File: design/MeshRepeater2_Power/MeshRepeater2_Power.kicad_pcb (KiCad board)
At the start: 2 copper layers, 90 x 60 mm, 121 parts, among them J101 INTERBOARD 2x6 VERTICAL, J12 LTO 2S + MID -, J7 SOLAR 12V, J8 Na-ion 1S, Q1 AO3401A, Q4 AO3401A, Q5 BSS138, Q6 AO3401A, Q7 AO3401A, U1 CN3722, U10 LM393XK, U11 LM285Z-2.5G, U12 INA219AIDR, U2 TPS63802DLAR, U8 LMV431A, U9 LMV431A

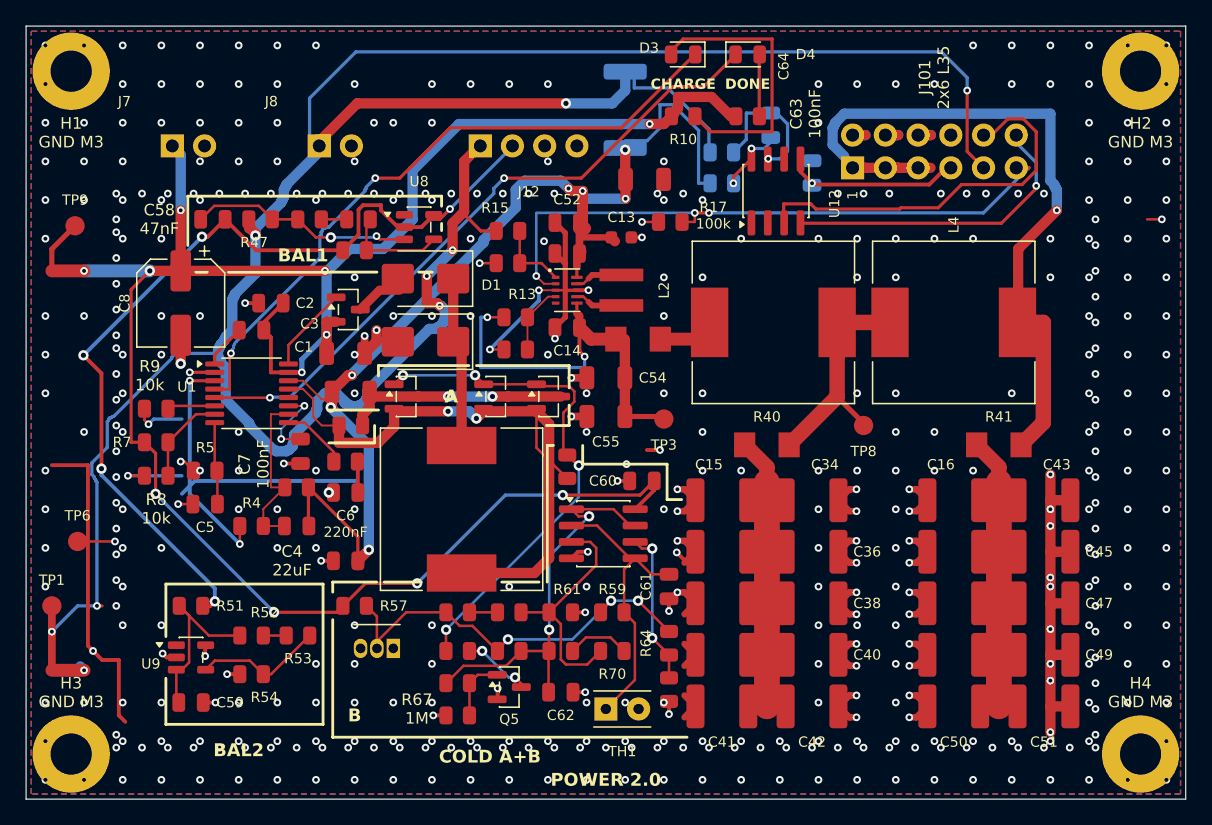
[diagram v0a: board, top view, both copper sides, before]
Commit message: Publish Mesh Repeater 2.0 A3 prototype and engineering audit
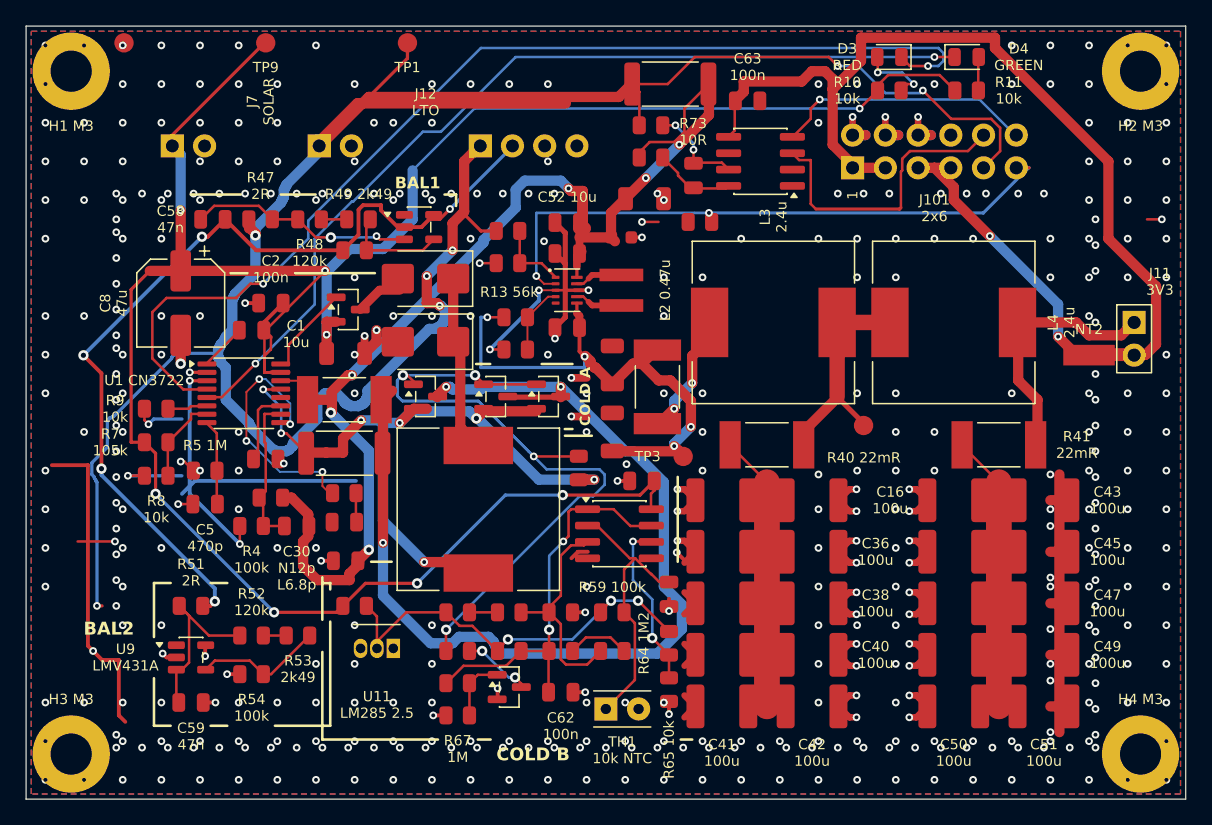
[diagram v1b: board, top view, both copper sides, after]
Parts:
- added J11: LC OUT - 3V3, Meshcore:Connfly_DS1022_1x02RUF11_B_Horizontal, F.Cu at (86.0, 23.0)
- added NT2: 3V3 STAR, Meshcore:NetTie_2_SMD_Power_Star_A3, F.Cu at (82.5, 25.5)
- C63, C64, R72, R73: moved to F.Cu
- J12: value LTO 2S + MID - -> LTO
- J8: value Na-ion 1S -> Na-ion
- R1: footprint Meshcore:R_1206_3216Metric__V2_R1 -> Meshcore:R_Vishay_WSL2512_A3__A3_R1
- R40: footprint Meshcore:R_Vishay_WSL1206_18__V2_R40 -> Meshcore:R_Vishay_WSL2512_A3__A3_R40
- R41: footprint Meshcore:R_Vishay_WSL1206_18__V2_R41 -> Meshcore:R_Vishay_WSL2512_A3__A3_R41
- R55: footprint Meshcore:R_Vishay_WSL1206_18__V2_R55 -> Meshcore:R_Vishay_WSL2512_A3__A3_R55
- R56: value 1.8 ohm 1% 0.125W -> 1.8R 1% 1W; footprint Meshcore:R_0805_2012Metric__V2_R56 -> Meshcore:R_2512_6332Metric__A3_R56
- R71: footprint Meshcore:R_2512_6332Metric__V2_R71 -> Meshcore:R_2512_6332Metric__A3_R71; moved to F.Cu
- TP1: footprint Meshcore:TestPoint_Pad_D1.5mm__V2_TP1 -> Meshcore:TestPoint_Pad_D1p5mm_A3_Edge_R0p9
- TP6: footprint Meshcore:TestPoint_Pad_D1.5mm__V2_TP6 -> Meshcore:TestPoint_Pad_D1p5mm_A3_Edge_R0p9
- TP9: footprint Meshcore:TestPoint_Pad_D1.5mm__V2_TP9 -> Meshcore:TestPoint_Pad_D1p5mm_A3_Edge_R0p9
- moved TP1 51.7 mm to (29.6, 1.30)
- moved TP6 38.9 mm to (7.60, 1.30)
- moved TP9 20.5 mm to (18.6, 1.30)
- moved R11 17.1 mm to (73.0, 5.00)
- moved D4 17.0 mm to (73.0, 2.40)
- moved R10 16.1 mm to (67.0, 5.00)
- moved D3 16.0 mm to (67.0, 2.40)
- moved C63 7.51 mm to (56.0, 5.80), turned to 0 degrees
- moved C64 7.16 mm to (51.8, 11.6)
- moved R73 5.89 mm to (48.5, 7.70)
- moved R72 5.85 mm to (48.5, 10.2)
- moved R71 4.03 mm to (50.0, 4.50), turned to 180 degrees
- moved R55 3.99 mm to (49.0, 28.0), turned to -90 degrees
- moved TP3 3.26 mm to (51.0, 33.4)
- moved C7 2.77 mm to (18.6, 33.6), turned to 0 degrees
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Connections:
- J101 pad 1: FILTER_OUT -> SYS_3V3
- J101 pad 3: FILTER_OUT -> SYS_3V3
- J101 pad 5: FILTER_OUT -> RADIO_3V3
- J101 pad 7: SYS_3V3 -> RADIO_3V3
- J101 pad 8: GND -> unconnected-(J101-NC-Pad8)
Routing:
- net CHG_CS_M: track 17.8 -> 80.7 mm, vias 2 -> 3
- net SYS_3V3: track 13.8 -> 73.5 mm, vias 1 -> 0
- net FILTER_OUT: track 58.9 -> 19.9 mm, vias 1 -> 0
- net CHRG: track 51.3 -> 84.0 mm
- net CHG_G_SHUNT: track 40.2 -> 69.9 mm
- net BAT: track 213.4 -> 191.0 mm, vias 9 -> 7
- net SOLAR: track 165.7 -> 188.1 mm, vias 11 -> 8
- net RADIO_3V3: track 0.00 -> 21.6 mm, vias 0 -> 2
- net DONE: track 51.8 -> 72.0 mm
- net Net-(D3-A): track 22.2 -> 5.58 mm, vias 0 -> 2
- net Net-(U1-COM2): track 5.21 -> 19.8 mm, vias 0 -> 4
- net /2. Converter/SYS_PRE: track 31.3 -> 41.6 mm, vias 2 -> 4
- net CS_P: track 50.8 -> 60.3 mm, vias 2 -> 7
- net SDA: track 30.6 -> 23.1 mm
- net BAT_SYS: track 91.7 -> 99.0 mm, vias 7 -> 6
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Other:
- board text added: "1 BAT 2 MID 3 GND 4 NC"
- board text added: "C1 10u"
- board text added: "C12 10u"
- board text added: "C13 100n"
- board text added: "C14 22u"
- board text added: "C15 100u"
- board text added: "C16 100u"
- board text added: "C2 100n"
- board text added: "C3 100n"
- board text added: "C30 N12p L6.8p"
- board text added: "C34 100u"
- board text added: "C35 100u"
- board text added: "C36 100u"
- board text added: "C37 100u"
- board text added: "C38 100u"
- board text added: "C39 100u"
- board text added: "C4 22u"
- board text added: "C40 100u"
- board text added: "C41 100u"
- board text added: "C42 100u"
- board text added: "C43 100u"
- board text added: "C44 100u"
- board text added: "C45 100u"
- board text added: "C46 100u"
- board text added: "C47 100u"
- board text added: "C48 100u"
- board text added: "C49 100u"
- board text added: "C5 470p"
- board text added: "C50 100u"
- board text added: "C51 100u"
- board text added: "C52 10u"
- board text added: "C53 DNP"
- board text added: "C54 DNP"
- board text added: "C55 DNP"
- board text added: "C58 47n"
- board text added: "C59 47n"
- board text added: "C6 220n"
- board text added: "C60 100n"
- board text added: "C61 1n"
- board text added: "C62 100n"
- board text added: "C63 100n"
- board text added: "C64 100n"
- board text added: "C7 100n"
- board text added: "C8 47u"
- board text added: "COLD A"
- board text added: "COLD B"
- board text added: "H1 M3"
- board text added: "H2 M3"
- board text added: "H3 M3"
- board text added: "H4 M3"
- board text added: "J101 1/3 SYS 5/7 RADIO 2/4/6 GND 8 NC 9 BAT 10 SDA 11 MODE 12 SCL"
- board text added: "J101 2x6"
- board text added: "J11 1 LC 2 3V3"
- board text added: "J11 3V3"
- board text added: "J12 LTO"
- board text added: "J7 SOLAR 1 VIN 2 GND"
- board text added: "J8 Na-ion"
- board text added: "J8 Na-ion 1 BAT+ 2 GND"
- board text added: "L1 100u"
- board text added: "L2 0.47u"
- board text added: "L3 2.4u"
- board text added: "L4 2.4u"
- board text added: "Mesh Repeater ver 2.0 Designed by @Alksndritm"
- board text added: "N: Na-ion / L: LTO 2S"
- board text added: "NT2"
- board text added: "Q4 AO34 01A"
- board text added: "Q6 AO34 01A"
- board text added: "Q7 AO34 01A"
- board text added: "R1 0R28"
- board text added: "R15 N40k2 L130k"
- board text added: "R16 49k9"
- board text added: "R3 N61k9 L121k"
- board text added: "R4 100k"
- board text added: "R49 2k49"
- board text added: "R53 2k49"
- board text added: "R56 1R8/0R"
- board text added: "R56: 0R без ХОЛОДА"
- board text added: "R64 1M2"
- board text added: "R71 0R1"
- board text added: "U10 LM393"
- board text added: "U11 LM285 2.5"
- board text added: "U12 INA219"
- board text added: "U2 TPS6 3802"
- board text added: "USB: снять J11"
- board text removed: "1 BAT+"
- board text removed: "1 LC_OUT"
- board text removed: "1 NTC"
- board text removed: "1 SOLAR+"
- board text removed: "10 SDA"
- board text removed: "11 MODE"
- board text removed: "12 SCL"
- board text removed: "2 GND"
- board text removed: "2 MID"
- board text removed: "3 GND"
- board text removed: "3 LC_OUT"
- board text removed: "4 GND"
- board text removed: "4 NC"
- board text removed: "5 LC_OUT"
- board text removed: "6 GND"
- board text removed: "7 SYS_3V3"
- board text removed: "8 GND"
- board text removed: "9 BAT"
- board text removed: "A"
- board text removed: "B"
- board text removed: "C1"
- board text removed: "C1 10uF"
- board text removed: "C12 10uF"
- board text removed: "C13"
- board text removed: "C13 100nF"
- board text removed: "C14"
- board text removed: "C14 22uF"
- board text removed: "C15"
- board text removed: "C15 100uF"
- board text removed: "C16"
- board text removed: "C16 100uF"
- board text removed: "C2"
- board text removed: "C2 100nF"
- board text removed: "C3"
- board text removed: "C3 100nF"
- board text removed: "C30 Na:12pF LTO:6.8pF"
- board text removed: "C34"
- board text removed: "C34 100uF"
- board text removed: "C35 100uF"
- board text removed: "C36"
- board text removed: "C36 100uF"
- board text removed: "C37 100uF"
- board text removed: "C38"
- board text removed: "C38 100uF"
- board text removed: "C39 100uF"
- board text removed: "C4 22uF"
- board text removed: "C40"
- board text removed: "C40 100uF"
- board text removed: "C41"
- board text removed: "C41 100uF"
- board text removed: "C42"
- board text removed: "C42 100uF"
- board text removed: "C43"
- board text removed: "C43 100uF"
- board text removed: "C44 100uF"
- board text removed: "C45"
- board text removed: "C45 100uF"
- board text removed: "C46 100uF"
- board text removed: "C47"
- board text removed: "C47 100uF"
- board text removed: "C48 100uF"
- board text removed: "C49"
- board text removed: "C49 100uF"
- board text removed: "C5"
- board text removed: "C5 470pF"
- board text removed: "C50"
- board text removed: "C50 100uF"
- board text removed: "C51"
- board text removed: "C51 100uF"
- board text removed: "C52"
- board text removed: "C52 10uF"
- board text removed: "C53"
- board text removed: "C54"
- board text removed: "C55"
- board text removed: "C58 47nF"
- board text removed: "C59"
- board text removed: "C59 47nF"
- board text removed: "C6 220nF"
- board text removed: "C60"
- board text removed: "C60 100nF"
- board text removed: "C61"
- board text removed: "C61 1nF"
- board text removed: "C62"
- board text removed: "C62 100nF"
- board text removed: "C63 100nF"
- board text removed: "C64"
- board text removed: "C64 100nF"
- board text removed: "C7 100nF"
- board text removed: "C8"
- board text removed: "C8 47uF"
- board text removed: "CHARGE"
- board text removed: "COLD A+B"
- board text removed: "D1"
- board text removed: "D3"
- board text removed: "D4"
- board text removed: "DONE"
- board text removed: "G1 x4"
- board text removed: "G10 x1.5"
- board text removed: "G11 x1.5"
- board text removed: "G12 x1.5"
- board text removed: "G13 x1.5"
- board text removed: "G14 x1.5"
- board text removed: "G2 x2"
- board text removed: "G3 x1.5"
- board text removed: "G4 x2"
- board text removed: "G5 x1.5"
- board text removed: "G6 x3"
- board text removed: "G7 x2"
- board text removed: "G8 x1.5"
- board text removed: "G9 x2"
- board text removed: "H1 GND M3"
- board text removed: "H2 GND M3"
- board text removed: "H3 GND M3"
- board text removed: "H4 GND M3"
- board text removed: "J101 2x6 L35"
- board text removed: "J12"
- board text removed: "J12 BAT/MID"
- board text removed: "J7"
- board text removed: "J8"
- board text removed: "J8 BAT"
- board text removed: "L1 100uH"
- board text removed: "L2"
- board text removed: "L2 0.47uH"
- board text removed: "L3 2.4uH"
- board text removed: "L4"
- board text removed: "L4 2.4uH"
- board text removed: "POWER 2.0"
- board text removed: "Q4 AO3401A"
- board text removed: "Q5"
- board text removed: "Q6 AO3401A"
- board text removed: "Q7 AO3401A"
- board text removed: "R1 0.28R"
- board text removed: "R10"
- board text removed: "R13"
- board text removed: "R15"
- board text removed: "R15 Na:40.2k LTO:130k"
- board text removed: "R16 Na:49.9k LTO:49.9k"
- board text removed: "R3 Na:61.9k LTO:121k"
- board text removed: "R4"
- board text removed: "R4 Na:100k LTO:100k"
- board text removed: "R40"
- board text removed: "R41"
- board text removed: "R47"
- board text removed: "R49 2.49k"
- board text removed: "R5"
- board text removed: "R51"
- board text removed: "R52"
- board text removed: "R53"
- board text removed: "R53 2.49k"
- board text removed: "R54"
- board text removed: "R56 Na:1.8R LTO:0R"
- board text removed: "R57"
- board text removed: "R59"
- board text removed: "R61"
- board text removed: "R64"
- board text removed: "R64 1.2M"
- board text removed: "R7"
- board text removed: "R70"
- board text removed: "R71 0.1R"
- board text removed: "TH1"
- board text removed: "U1"
- board text removed: "U10 LM393XK"
- board text removed: "U11 LM285Z-2.5G"
- board text removed: "U12"
- board text removed: "U12 INA219AIDR"
- board text removed: "U2 TPS63802DLAR"
- board text removed: "U8"
- board text removed: "U9"

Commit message: Publish Mesh Repeater 2.0 A4 with consistent silkscreen and clean current CAD
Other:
- board text added: "C15, C34-C42 10x100uF"
- board text added: "C16, C43-C51 10x100uF"
- board text added: "J12 LTO 1 BAT 2 MID 3 GND 4 NC"
- board text added: "R56 N1R8 L0R"
- board text added: "U2 TPS63802"
- board text removed: "1 BAT 2 MID 3 GND 4 NC"
- board text removed: "C15 100u"
- board text removed: "C16 100u"
- board text removed: "C34 100u"
- board text removed: "C35 100u"
- board text removed: "C36 100u"
- board text removed: "C37 100u"
- board text removed: "C38 100u"
- board text removed: "C39 100u"
- board text removed: "C40 100u"
- board text removed: "C41 100u"
- board text removed: "C42 100u"
- board text removed: "C43 100u"
- board text removed: "C44 100u"
- board text removed: "C45 100u"
- board text removed: "C46 100u"
- board text removed: "C47 100u"
- board text removed: "C48 100u"
- board text removed: "C49 100u"
- board text removed: "C50 100u"
- board text removed: "C51 100u"
- board text removed: "J101 2x6"
- board text removed: "J11 3V3"
- board text removed: "J12 LTO"
- board text removed: "J7 SOLAR"
- board text removed: "J8 Na-ion"
- board text removed: "R56 1R8/0R"
- board text removed: "U2 TPS6 3802"

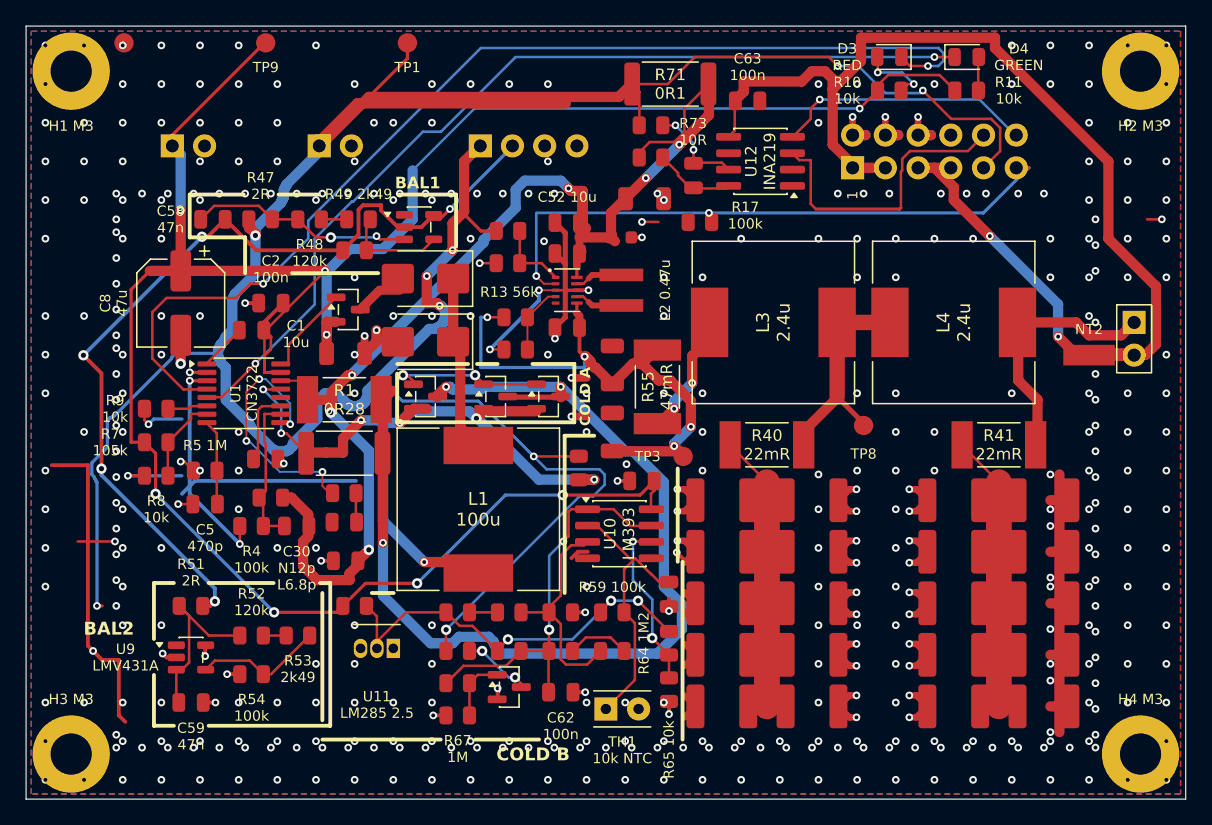
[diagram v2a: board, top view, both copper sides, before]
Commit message: Publish A5 routing fixes and CC BY-NC-SA licensing
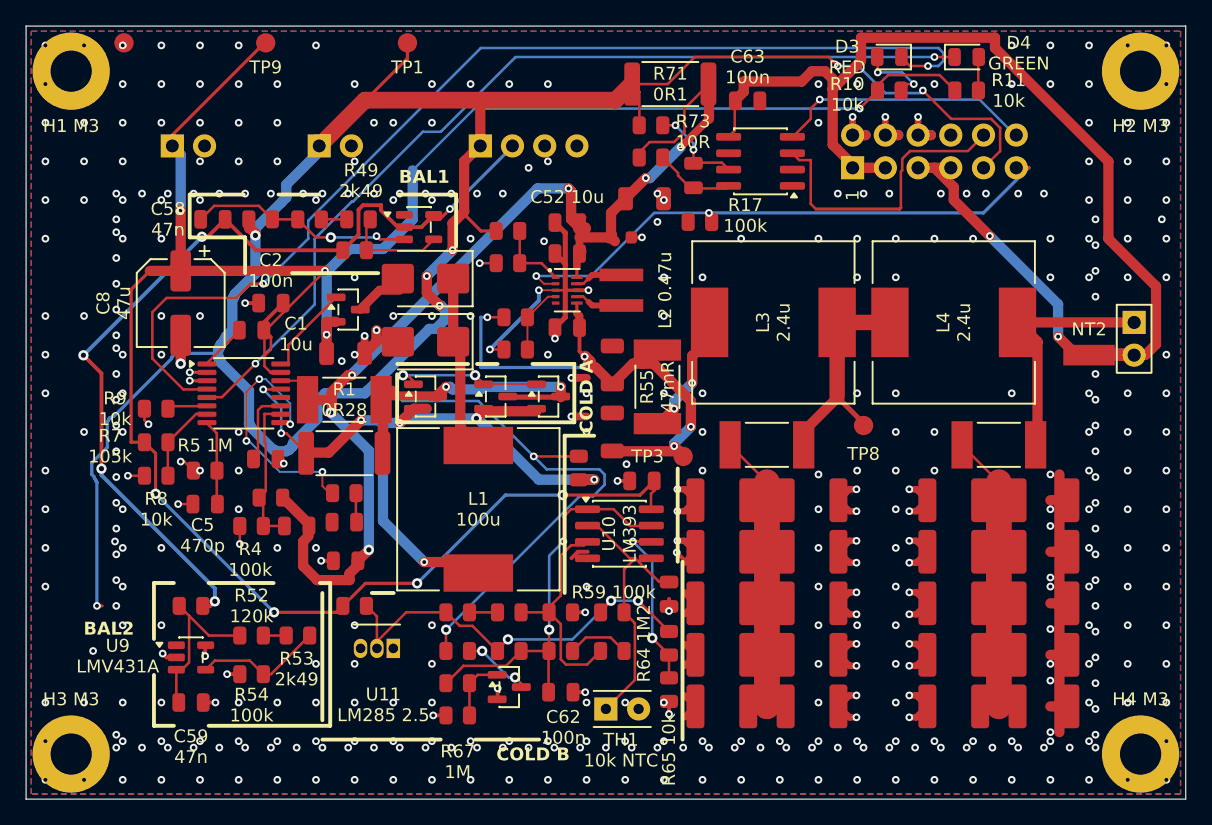
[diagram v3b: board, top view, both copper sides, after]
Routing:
- net GND: track 209.9 -> 144.4 mm, vias 435 -> 433
- net CHG_CS_M: track 80.7 -> 24.1 mm, vias 3 -> 2
- net BAT: track 191.0 -> 172.3 mm
- net CHG_G_SHUNT: track 69.9 -> 55.6 mm
- net BAT_SYS: track 99.0 -> 93.7 mm
- net MODE: track 48.3 -> 45.4 mm
- net SYS_3V3: track 73.5 -> 71.0 mm
- net SOLAR: track 188.1 -> 186.0 mm
- net CS_P: track 60.3 -> 59.2 mm
- net Net-(U9-K): track 14.2 -> 13.1 mm
- net FILTER_OUT: track 19.9 -> 19.1 mm
- net /4. Thermal/CHG_VREF: track 32.9 -> 32.4 mm
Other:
- board text added: "Q4"
- board text added: "Q4,Q6,Q7 AO3401A"
- board text added: "Q5 BSS 138"
- board text added: "Q6"
- board text added: "Q7"
- board text removed: "Q4 AO34 01A"
- board text removed: "Q5 BSS138"
- board text removed: "Q6 AO34 01A"
- board text removed: "Q7 AO34 01A"
